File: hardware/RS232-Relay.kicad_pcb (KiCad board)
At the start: 2 copper layers, 82.5 x 151 mm, 171 parts, among them J10 Relay 1-4, J11 Relay 1-4, J2 Conn_01x02, J4 Conn_01x09, J5 Conn_01x09, J7 RS232_1, J8 RS232_2, J9 Relay 1-4, K1 G5V-1, K13 G5V-1, K14 G5V-1, K15 G5V-1, K2 G5V-1, K3 G5V-1, K4 G5V-1, K5 G5V-1, K6 G5V-1, K7 G5V-1, K8 G5V-1, K9 G5V-1, Q1 2N3904, Q13 2N3904, Q14 2N3904, Q15 2N3904, Q2 2N3904, Q3 2N3904, Q4 2N3904, Q5 2N3904, Q6 2N3904, Q7 2N3904, Q8 2N3904, Q9 2N3904, SW2 SW_SPST, SW3 SW_SPST, U1 TEC2-1210WI, U2 LTV-847S, U3 PCF8575DBR, U4 MAX3232, U5 LTV-847S, U6 LTV-847S

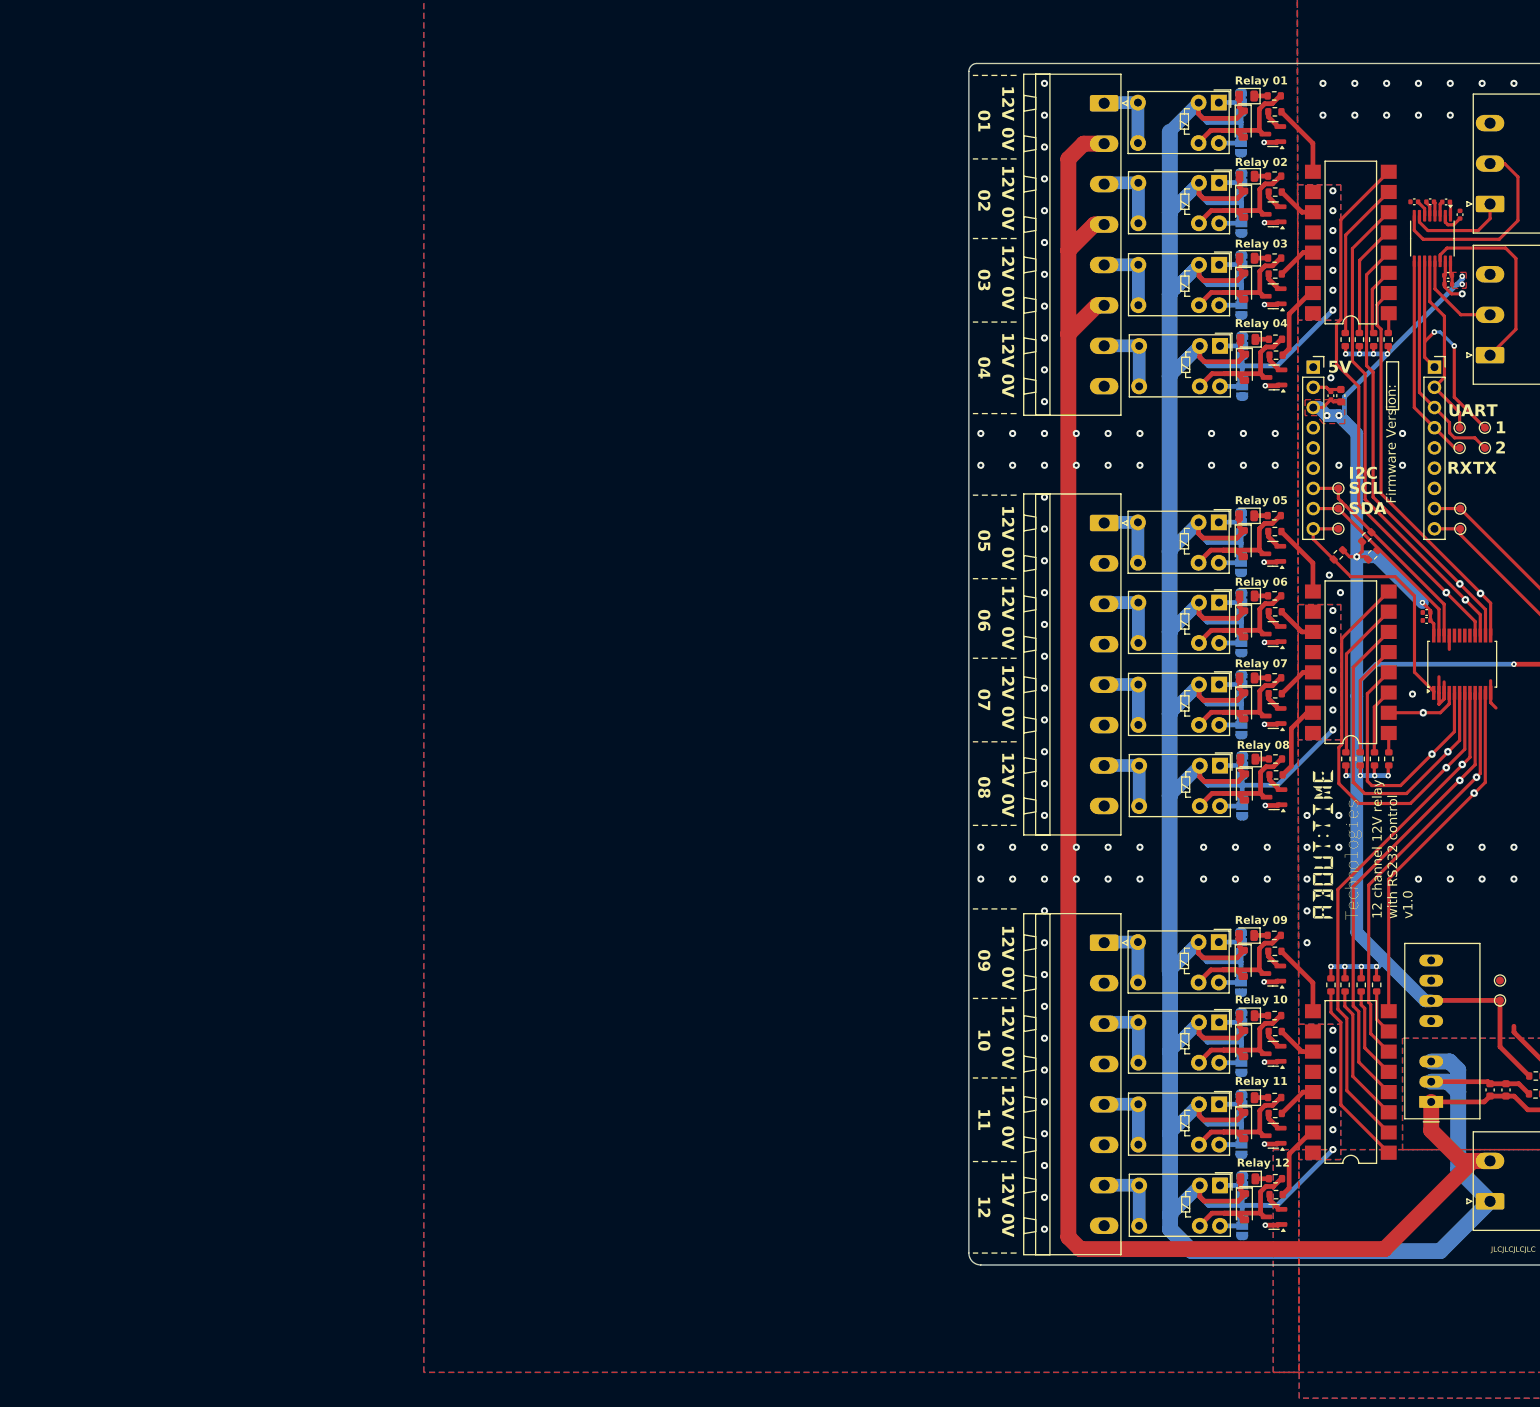
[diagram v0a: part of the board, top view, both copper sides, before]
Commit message: Transitioning to more robust circuit
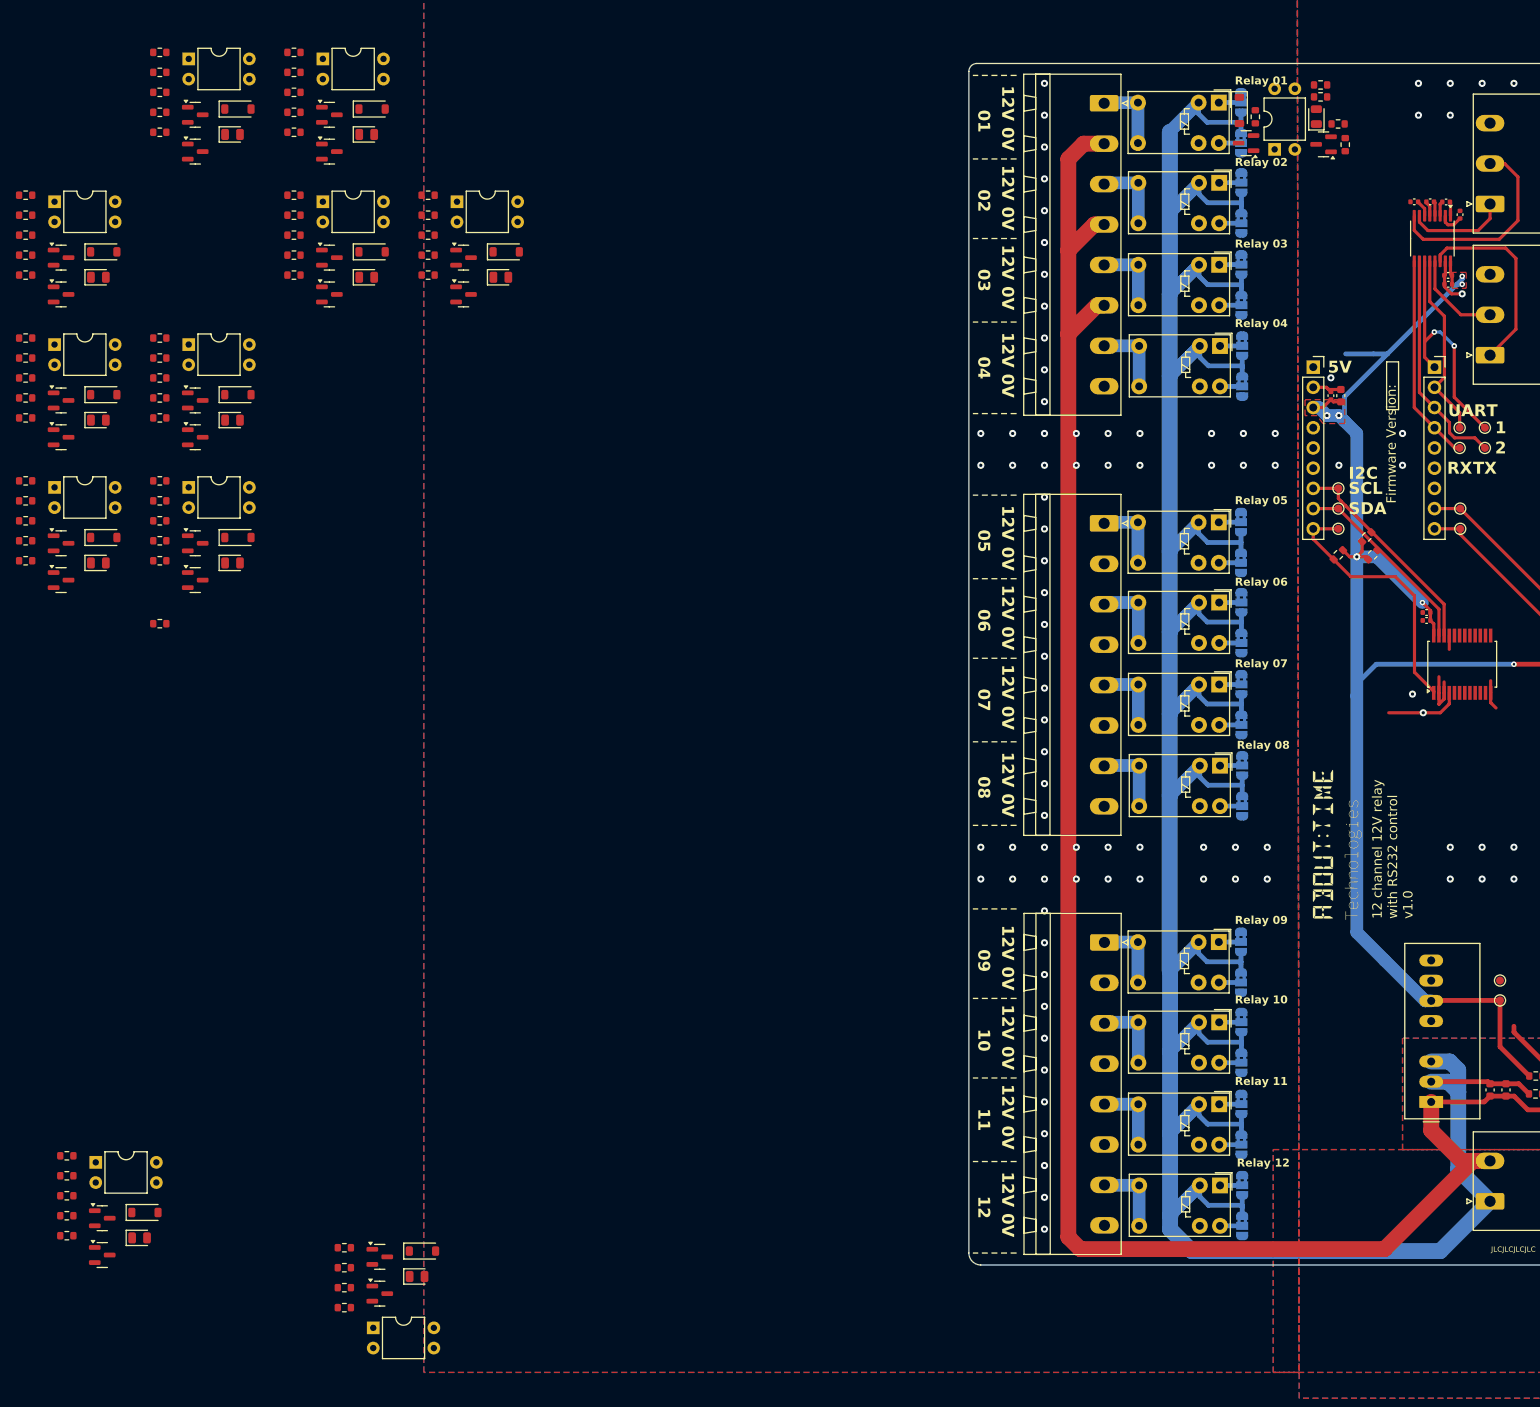
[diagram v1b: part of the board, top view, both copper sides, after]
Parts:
- removed D28, D30, D32: RED, LED_SMD:LED_0805_2012Metric
- removed J10, J11, J9: Relay 1-4, Connector_Phoenix_MSTB:PhoenixContact_MSTBA_2,5_8-G-5,08_1x08_P5.08mm_Horizontal
- removed TP14, TP15, TP16, TP17, TP18, TP19, TP2, TP20, TP21, TP22, TP23, TP3: Backup, TestPoint:TestPoint_Pad_D1.0mm
- added D22: RED, LED_SMD:LED_0805_2012Metric, F.Cu at (-7.18, 44.4)
- added D23: RED, LED_SMD:LED_0805_2012Metric, F.Cu at (-24.0, 80.3)
- added D7: RED, LED_SMD:LED_0805_2012Metric, F.Cu at (-24.0, 98.3)
- added J1: Conn_01x08, Header:PhoenixContact_MSTBA_2,5_8-G-5,08_1x08_P5.08mm_Horizontal, F.Cu at (85.5, 40.5)
- added J3: Conn_01x08, Header:PhoenixContact_MSTBA_2,5_8-G-5,08_1x08_P5.08mm_Horizontal, F.Cu at (85.5, 146.0)
- added J6: Conn_01x08, Header:PhoenixContact_MSTBA_2,5_8-G-5,08_1x08_P5.08mm_Horizontal, F.Cu at (85.5, 93.3)
- added Q10: SS8050, Package_TO_SOT_SMD:SOT-23, F.Cu at (103.3, 45.5)
- added Q11: SS8050, Package_TO_SOT_SMD:SOT-23, F.Cu at (-5.54, 190.1)
- added Q12: SS8050, Package_TO_SOT_SMD:SOT-23, F.Cu at (-28.7, 100.4)
- added Q16: SS8050, Package_TO_SOT_SMD:SOT-23, F.Cu at (-45.6, 82.5)
- added Q17: SS8050, Package_TO_SOT_SMD:SOT-23, F.Cu at (-28.7, 46.6)
- added Q18: SS8050, Package_TO_SOT_SMD:SOT-23, F.Cu at (4.99, 64.5)
- added Q19: SS8050, Package_TO_SOT_SMD:SOT-23, F.Cu at (-45.6, 64.5)
- added Q20: SS8050, Package_TO_SOT_SMD:SOT-23, F.Cu at (-40.4, 185.2)
- added Q21: SS8050, Package_TO_SOT_SMD:SOT-23, F.Cu at (-11.9, 64.5)
- added Q22: SS8050, Package_TO_SOT_SMD:SOT-23, F.Cu at (-45.6, 100.4)
- added Q23: SS8050, Package_TO_SOT_SMD:SOT-23, F.Cu at (-11.9, 46.6)
- added Q24: SS8050, Package_TO_SOT_SMD:SOT-23, F.Cu at (-28.7, 82.5)
- added R35: 4.7kR, Resistor_SMD:R_0603_1608Metric, F.Cu at (-50.0, 57.1)
- added R36: 4.7kR, Resistor_SMD:R_0603_1608Metric, F.Cu at (-44.9, 177.8)
- added R37: 4.7kR, Resistor_SMD:R_0603_1608Metric, F.Cu at (-16.3, 57.1)
- added R38: 4.7kR, Resistor_SMD:R_0603_1608Metric, F.Cu at (-50.0, 90.5)
- added R39: 4.7kR, Resistor_SMD:R_0603_1608Metric, F.Cu at (-16.3, 36.6)
- added R40: 4.7kR, Resistor_SMD:R_0603_1608Metric, F.Cu at (-33.2, 72.5)
- added R41: 4.7kR, Resistor_SMD:R_0603_1608Metric, F.Cu at (115.8, 45.7)
- added R42: 4.7kR, Resistor_SMD:R_0603_1608Metric, F.Cu at (-9.99, 189.3)
- added R43: 4.7kR, Resistor_SMD:R_0603_1608Metric, F.Cu at (-33.2, 95.5)
- added R53: 4.7kR, Resistor_SMD:R_0603_1608Metric, F.Cu at (-50.0, 95.5)
- added R54: 4.7kR, Resistor_SMD:R_0603_1608Metric, F.Cu at (-16.3, 41.6)
- added R55: 4.7kR, Resistor_SMD:R_0603_1608Metric, F.Cu at (-33.2, 77.5)
- added R56: 100kR, Resistor_SMD:R_0603_1608Metric, F.Cu at (114.9, 43.1)
- added R57: 100kR, Resistor_SMD:R_0603_1608Metric, F.Cu at (-9.99, 191.9)
- added R58: 100kR, Resistor_SMD:R_0603_1608Metric, F.Cu at (-33.2, 98.0)
- added R59: 100kR, Resistor_SMD:R_0603_1608Metric, F.Cu at (-50.0, 80.0)
- added R60: 100kR, Resistor_SMD:R_0603_1608Metric, F.Cu at (-33.2, 44.1)
- added R61: 100kR, Resistor_SMD:R_0603_1608Metric, F.Cu at (0.54, 62.1)
- added R62: 100kR, Resistor_SMD:R_0603_1608Metric, F.Cu at (-50.0, 62.1)
- added R63: 100kR, Resistor_SMD:R_0603_1608Metric, F.Cu at (-44.9, 182.8)
- added R64: 100kR, Resistor_SMD:R_0603_1608Metric, F.Cu at (-16.3, 62.1)
- added R65: 100kR, Resistor_SMD:R_0603_1608Metric, F.Cu at (-50.0, 98.0)
- added R66: 100kR, Resistor_SMD:R_0603_1608Metric, F.Cu at (-16.3, 44.1)
- added R67: 100kR, Resistor_SMD:R_0603_1608Metric, F.Cu at (-33.2, 80.0)
- added U10: PC817, Package_DIP:DIP-4_W7.62mm, F.Cu at (-46.4, 52.9)
- added U11: PC817, Package_DIP:DIP-4_W7.62mm, F.Cu at (-41.2, 173.6)
- added U12: PC817, Package_DIP:DIP-4_W7.62mm, F.Cu at (-12.7, 52.9)
- added U13: PC817, Package_DIP:DIP-4_W7.62mm, F.Cu at (-46.4, 88.8)
- added U14: PC817, Package_DIP:DIP-4_W7.62mm, F.Cu at (-12.7, 34.9)
- added U15: PC817, Package_DIP:DIP-4_W7.62mm, F.Cu at (-29.6, 70.8)
- added U7: PC817, Package_DIP:DIP-4_W7.62mm, F.Cu at (-46.4, 70.8)
- added U8: PC817, Package_DIP:DIP-4_W7.62mm, F.Cu at (-29.6, 34.9)
- added U9: PC817, Package_DIP:DIP-4_W7.62mm, F.Cu at (4.17, 52.9)
- Q1, Q13, Q14, Q15, Q2, Q3, Q4, Q5, Q6, Q7, Q8, Q9: value 2N3904 -> SS8050
- R10: value 51R -> 2000R
- R11, R14, R17, R20, R23: value 1000R -> 2000R
- R12, R15, R18, R21, R24, R3: value 220R -> 2000R
- R13, R16, R19, R22, R25, R28, R31, R34, R46, R49, R5, R52: value 660R -> 4.7kR
- R26, R29, R32, R44, R47, R50: value 1000R -> 4.7kR
- R27, R30, R33, R45, R48, R51: value 220R -> 4.7kR
- U2, U5, U6: value LTV-847S -> PC817; footprint Package_DIP:SMDIP-16_W9.53mm -> Package_DIP:DIP-4_W7.62mm
- moved R18 193.6 mm to (-44.9, 172.8), turned to 0 degrees
- moved R48 193.0 mm to (-50.0, 59.6), turned to 0 degrees
- moved R22 191.8 mm to (-33.2, 36.6), turned to 0 degrees
- moved Q5 186.6 mm to (-28.7, 42.0), turned to 0 degrees
- moved R12 186.5 mm to (-50.0, 70.0), turned to 0 degrees
- moved R30 180.9 mm to (-50.0, 75.0), turned to 0 degrees
- moved D16 179.3 mm to (-35.7, 183.1), turned to 0 degrees
- moved R21 177.5 mm to (-50.0, 88.0), turned to 0 degrees
- moved D19 176.2 mm to (-6.50, 41.2), turned to 0 degrees
- moved R27 175.5 mm to (-9.99, 186.8), turned to 0 degrees
- moved R50 175.4 mm to (-44.9, 180.3)
- moved D4 172.5 mm to (-23.4, 41.2), turned to 0 degrees
- moved R20 167.5 mm to (-16.3, 52.1)
- moved R46 165.2 mm to (-50.0, 93.0), turned to 0 degrees
- moved R49 163.9 mm to (-16.3, 39.1), turned to 0 degrees
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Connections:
- D1 pad 2: +12V -> Net-(D1-A)
- D10 pad 2: +12V -> Net-(D10-A)
- D12 pad 2: +12V -> Net-(D12-A)
- D14 pad 2: +12V -> Net-(D14-A)
- D16 pad 2: +12V -> Net-(D16-A)
- D18 pad 2: +12V -> Net-(D18-A)
- D20 pad 2: +12V -> Net-(D20-A)
- D3 pad 2: +12V -> Net-(D3-A)
- D8 pad 2: +12V -> Net-(D8-A)
- Q1 pad 1: GND -> Net-(Q1-B)
- Q1 pad 2: Net-(Q1-B) -> GNDREF
- Q1 pad 3: Net-(D2-A) -> Net-(D1-K)
- Q13 pad 1: GND -> Net-(Q13-B)
- Q13 pad 2: Net-(Q13-B) -> GNDREF
- Q13 pad 3: Net-(D29-A) -> Net-(D20-K)
- Q14 pad 1: GND -> Net-(Q14-B)
- Q14 pad 2: Net-(Q14-B) -> GNDREF
- Q14 pad 3: Net-(D31-A) -> Net-(D22-K)
- Q15 pad 1: GND -> Net-(Q15-B)
- Q15 pad 2: Net-(Q15-B) -> GNDREF
- Q15 pad 3: Net-(D33-A) -> Net-(D23-K)
- Q2 pad 1: GND -> Net-(Q2-B)
- Q2 pad 2: Net-(Q2-B) -> GNDREF
- Q2 pad 3: Net-(D4-A) -> Net-(D3-K)
- Q3 pad 1: GND -> Net-(Q3-B)
- Q3 pad 2: Net-(Q3-B) -> GNDREF
- Q3 pad 3: Net-(D9-A) -> Net-(D7-K)
- Q4 pad 1: GND -> Net-(Q4-B)
- Q4 pad 2: Net-(Q4-B) -> GNDREF
- Q4 pad 3: Net-(D11-A) -> Net-(D8-K)
- Q5 pad 1: GND -> Net-(Q5-B)
- Q5 pad 2: Net-(Q5-B) -> GNDREF
- Q5 pad 3: Net-(D13-A) -> Net-(D10-K)
- Q6 pad 1: GND -> Net-(Q6-B)
- Q6 pad 2: Net-(Q6-B) -> GNDREF
- Q6 pad 3: Net-(D15-A) -> Net-(D12-K)
- Q7 pad 1: GND -> Net-(Q7-B)
- Q7 pad 2: Net-(Q7-B) -> GNDREF
- Q7 pad 3: Net-(D17-A) -> Net-(D14-K)
- Q8 pad 1: GND -> Net-(Q8-B)
- Q8 pad 2: Net-(Q8-B) -> GNDREF
- Q8 pad 3: Net-(D19-A) -> Net-(D16-K)
- Q9 pad 1: GND -> Net-(Q9-B)
- Q9 pad 2: Net-(Q9-B) -> GNDREF
- Q9 pad 3: Net-(D21-A) -> Net-(D18-K)
- R10 pad 1: Net-(D6-A) -> +3V3
- R10 pad 2: +3V3 -> Net-(D3-A)
- R11 pad 1: Net-(D3-K) -> +3V3
- R11 pad 2: Net-(D4-A) -> Net-(D7-A)
- R12 pad 1: /Relay-Module1/Relay-NO-ISO1/OPTO_LEFT_IN -> +3V3
- R12 pad 2: +3V3 -> Net-(D8-A)
- R13 pad 1: /Relay-Module1/Relay-NO-ISO1/OPTO_RIGHT_OUT -> Net-(R13-Pad1)
- R13 pad 2: Net-(Q2-B) -> Net-(Q11-B)
- R14 pad 1: Net-(D8-K) -> +3V3
- R14 pad 2: Net-(D9-A) -> Net-(D10-A)
- R15 pad 1: /Relay-Module2/Relay-NO-ISO1/OPTO_LEFT_IN -> +3V3
- R15 pad 2: +3V3 -> Net-(D12-A)
- R16 pad 1: /Relay-Module2/Relay-NO-ISO1/OPTO_RIGHT_OUT -> Net-(R16-Pad1)
- R16 pad 2: Net-(Q3-B) -> Net-(Q12-B)
- R17 pad 1: Net-(D10-K) -> +3V3
- R17 pad 2: Net-(D11-A) -> Net-(D14-A)
- R18 pad 1: /Relay-Module/Relay-NO-ISO2/OPTO_LEFT_IN -> +3V3
- R18 pad 2: +3V3 -> Net-(D16-A)
- R19 pad 1: /Relay-Module/Relay-NO-ISO2/OPTO_RIGHT_OUT -> Net-(R19-Pad1)
- R19 pad 2: Net-(Q4-B) -> Net-(Q16-B)
- R2 pad 1: Net-(D1-K) -> +3V3
- R2 pad 2: Net-(D2-A) -> Net-(D6-A)
- R20 pad 1: Net-(D12-K) -> +3V3
- R20 pad 2: Net-(D13-A) -> Net-(D18-A)
- R21 pad 1: /Relay-Module1/Relay-NO-ISO2/OPTO_LEFT_IN -> +3V3
- R21 pad 2: +3V3 -> Net-(D20-A)
- R22 pad 1: /Relay-Module1/Relay-NO-ISO2/OPTO_RIGHT_OUT -> Net-(R22-Pad1)
- R22 pad 2: Net-(Q5-B) -> Net-(Q17-B)
- R23 pad 1: Net-(D14-K) -> +3V3
- R23 pad 2: Net-(D15-A) -> Net-(D22-A)
- R24 pad 1: /Relay-Module2/Relay-NO-ISO2/OPTO_LEFT_IN -> +3V3
- R24 pad 2: +3V3 -> Net-(D23-A)
- R25 pad 1: /Relay-Module2/Relay-NO-ISO2/OPTO_RIGHT_OUT -> Net-(R25-Pad1)
- R25 pad 2: Net-(Q6-B) -> Net-(Q18-B)
- R26 pad 1: Net-(D16-K) -> +3V3
- R26 pad 2: Net-(D17-A) -> Net-(R26-Pad2)
- R27 pad 1: /Relay-Module/Relay-NO-ISO3/OPTO_LEFT_IN -> +3V3
- R27 pad 2: +3V3 -> Net-(R27-Pad2)
- R28 pad 1: /Relay-Module/Relay-NO-ISO3/OPTO_RIGHT_OUT -> Net-(R28-Pad1)
- R28 pad 2: Net-(Q7-B) -> Net-(Q19-B)
- R29 pad 1: Net-(D18-K) -> +3V3
- R29 pad 2: Net-(D19-A) -> Net-(R29-Pad2)
- R3 pad 1: /Relay-Module/Relay-NO-ISO1/OPTO_LEFT_IN -> +3V3
- R3 pad 2: +3V3 -> Net-(D1-A)
- R30 pad 1: /Relay-Module1/Relay-NO-ISO3/OPTO_LEFT_IN -> +3V3
- R30 pad 2: +3V3 -> Net-(R30-Pad2)
- R31 pad 1: /Relay-Module1/Relay-NO-ISO3/OPTO_RIGHT_OUT -> Net-(R31-Pad1)
- R31 pad 2: Net-(Q8-B) -> Net-(Q20-B)
- R32 pad 1: Net-(D20-K) -> +3V3
- R32 pad 2: Net-(D21-A) -> Net-(R32-Pad2)
- R33 pad 1: /Relay-Module2/Relay-NO-ISO3/OPTO_LEFT_IN -> +3V3
- R33 pad 2: +3V3 -> Net-(R33-Pad2)
- R34 pad 1: /Relay-Module2/Relay-NO-ISO3/OPTO_RIGHT_OUT -> Net-(R34-Pad1)
- R34 pad 2: Net-(Q9-B) -> Net-(Q21-B)
- R44 pad 1: Net-(D28-K) -> RELAY_IN_02
- R44 pad 2: Net-(D29-A) -> Net-(Q4-B)
- R45 pad 1: /Relay-Module/Relay-NO-ISO/OPTO_LEFT_IN -> RELAY_IN_06
- R45 pad 2: +3V3 -> Net-(Q5-B)
- R46 pad 1: /Relay-Module/Relay-NO-ISO/OPTO_RIGHT_OUT -> Net-(R46-Pad1)
- R46 pad 2: Net-(Q13-B) -> Net-(Q22-B)
- R47 pad 1: Net-(D30-K) -> RELAY_IN_10
- R47 pad 2: Net-(D31-A) -> Net-(Q6-B)
- R48 pad 1: /Relay-Module1/Relay-NO-ISO/OPTO_LEFT_IN -> RELAY_IN_03
- R48 pad 2: +3V3 -> Net-(Q7-B)
- R49 pad 1: /Relay-Module1/Relay-NO-ISO/OPTO_RIGHT_OUT -> Net-(R49-Pad1)
- R49 pad 2: Net-(Q14-B) -> Net-(Q23-B)
- R5 pad 1: /Relay-Module/Relay-NO-ISO1/OPTO_RIGHT_OUT -> Net-(R5-Pad1)
- R5 pad 2: Net-(Q1-B) -> Net-(Q10-B)
- R50 pad 1: Net-(D32-K) -> RELAY_IN_07
- R50 pad 2: Net-(D33-A) -> Net-(Q8-B)
- R51 pad 1: /Relay-Module2/Relay-NO-ISO/OPTO_LEFT_IN -> RELAY_IN_11
- R51 pad 2: +3V3 -> Net-(Q9-B)
- R52 pad 1: /Relay-Module2/Relay-NO-ISO/OPTO_RIGHT_OUT -> Net-(R52-Pad1)
- R52 pad 2: Net-(Q15-B) -> Net-(Q24-B)
- U2 pad 1: /Relay-Module/Relay-NO-ISO3/OPTO_LEFT_IN -> Net-(R26-Pad2)
- U2 pad 2: RELAY_IN_04 -> Net-(D1-K)
- U2 pad 3: /Relay-Module/Relay-NO-ISO2/OPTO_LEFT_IN -> Net-(R5-Pad1)
- U2 pad 4: RELAY_IN_03 -> +12V
- U5 pad 1: /Relay-Module1/Relay-NO-ISO3/OPTO_LEFT_IN -> Net-(R27-Pad2)
- U5 pad 2: RELAY_IN_08 -> Net-(D3-K)
- U5 pad 3: /Relay-Module1/Relay-NO-ISO2/OPTO_LEFT_IN -> Net-(R13-Pad1)
- U5 pad 4: RELAY_IN_07 -> +12V
- U6 pad 1: /Relay-Module2/Relay-NO-ISO3/OPTO_LEFT_IN -> Net-(R29-Pad2)
- U6 pad 2: RELAY_IN_12 -> Net-(D7-K)
- U6 pad 3: /Relay-Module2/Relay-NO-ISO2/OPTO_LEFT_IN -> Net-(R16-Pad1)
- U6 pad 4: RELAY_IN_11 -> +12V
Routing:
- net +12V: track 575.2 -> 414.7 mm, vias 21 -> 0
- net RELAY_IN_01: track 68.2 -> 0.00 mm, vias 1 -> 0
- net RELAY_IN_08: track 64.8 -> 0.00 mm, vias 1 -> 0
- net RELAY_IN_02: track 61.8 -> 0.00 mm, vias 1 -> 0
- net RELAY_IN_07: track 58.4 -> 0.00 mm, vias 1 -> 0
- net RELAY_IN_03: track 55.5 -> 0.00 mm, vias 1 -> 0
- net RELAY_IN_09: track 53.5 -> 0.00 mm, vias 1 -> 0
- net RELAY_IN_06: track 51.9 -> 0.00 mm, vias 1 -> 0
- net RELAY_IN_04: track 49.6 -> 0.00 mm, vias 1 -> 0
- net RELAY_IN_05: track 45.4 -> 0.00 mm, vias 1 -> 0
- net RELAY_IN_10: track 43.5 -> 0.00 mm, vias 1 -> 0
- net RELAY_IN_11: track 33.6 -> 0.00 mm, vias 1 -> 0
- net +3V3: track 231.8 -> 203.8 mm, vias 21 -> 9
- net /Relay-Module1/Relay-NO-ISO3/OPTO_LEFT_IN: track 23.1 -> 0.00 mm
- net GND: track 263.9 -> 242.6 mm, vias 81 -> 69
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- removed copper zone on B.Cu, net +12V
- removed copper zone on F.Cu, net +12V
